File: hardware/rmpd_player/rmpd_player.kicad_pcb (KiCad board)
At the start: 2 copper layers, 99.7 x 67.9 mm, 142 parts, among them J1 POWER, J2 PROG, J3 LINE_OUT_INT_1, J4 LINE_OUT, J5 MICRO_SD, J6 POWER_INT, J7 LINE_OUT_INT_2, J8 RESERV, Q1 BC848, Q2 BC848, Q3 BC858, Q4 BC858, U1 DS3231M, U2 VS1011E, U3 LM1117-3.3, U4 ESP32-WROOM, U5 RC4558, U6 RC4558, U7 RC4558, U8 TPS54331D, U9 TPS54331D, Y1 12.288MHz

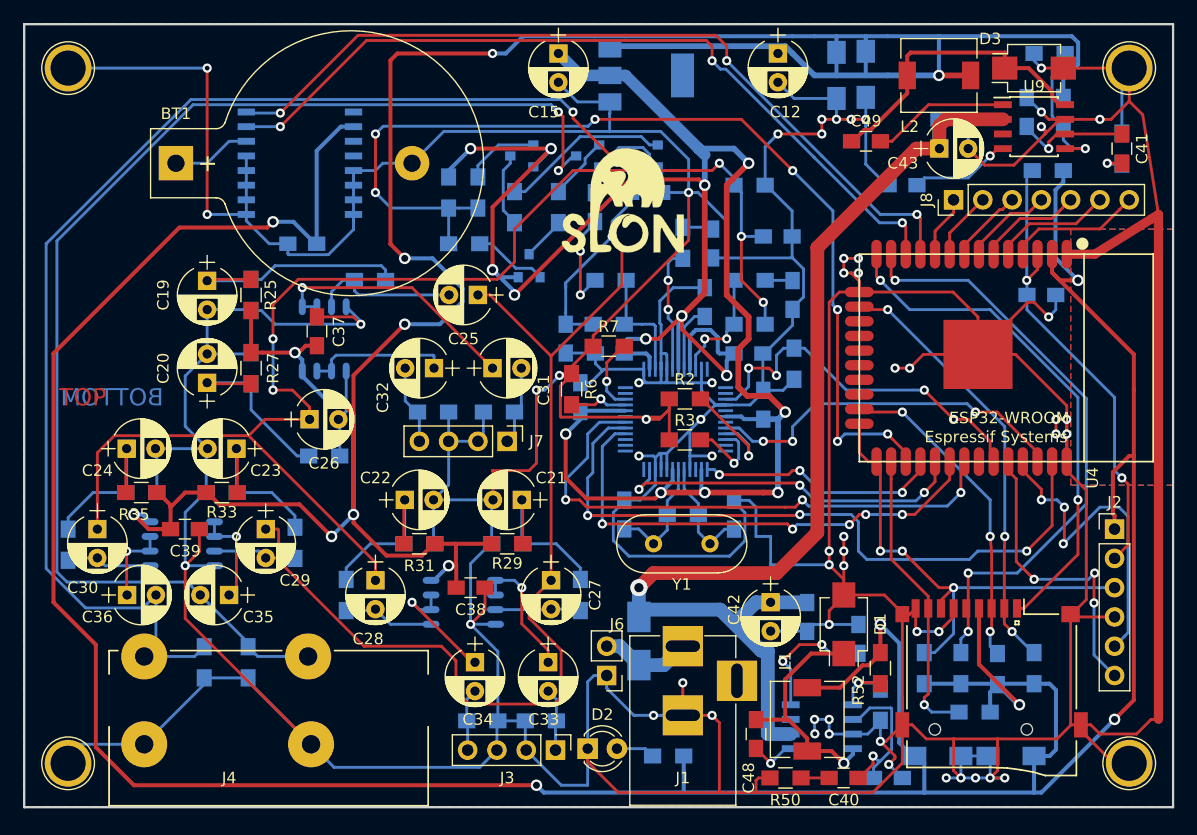
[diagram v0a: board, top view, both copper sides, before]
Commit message: update footprints to reflow
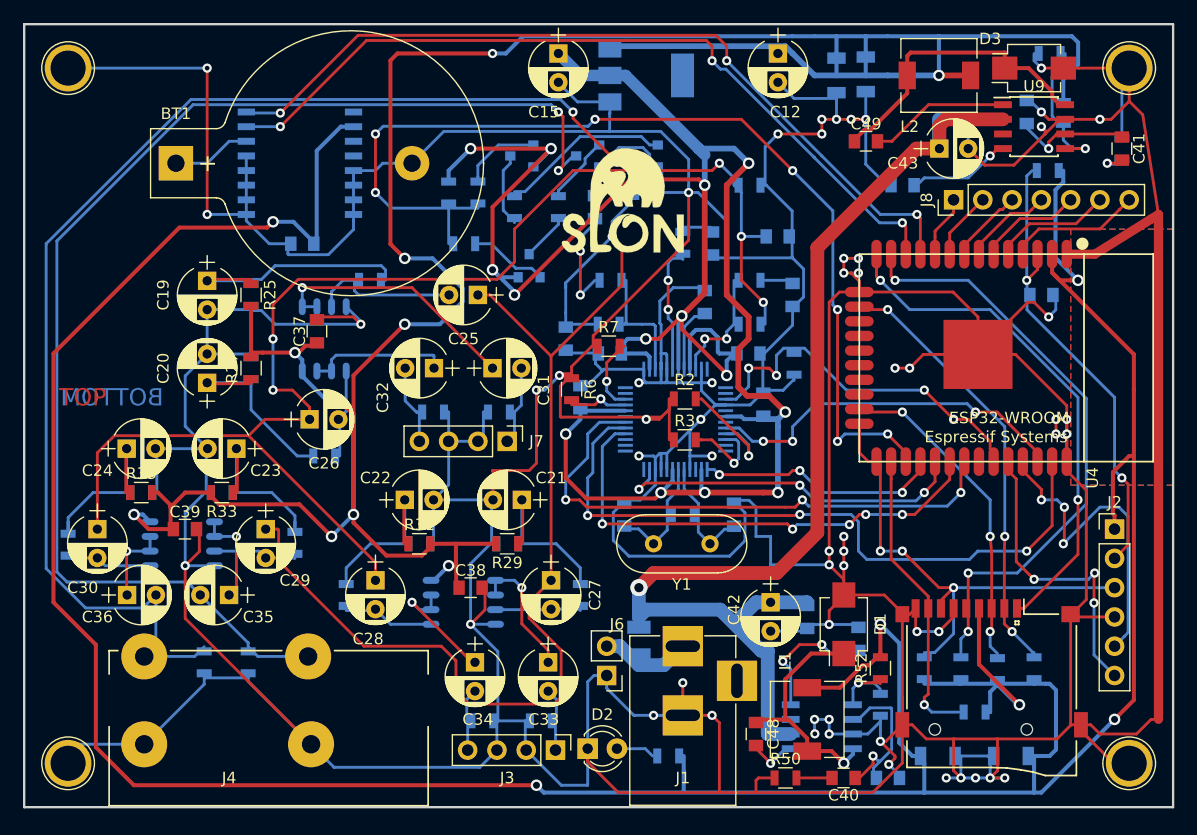
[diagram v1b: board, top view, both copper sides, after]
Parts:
- C1, C10, C11, C13, C14, C16, C2, C3, C37, C38, C39, C4, C40, C41, C44, C45, C48, C49, C5, C6, C7, C9: footprint Capacitors_SMD:C_0805_HandSoldering -> Capacitors_SMD:C_0805
- C17, C18, C46, C47: value 0.01 -> 10n; footprint Capacitors_SMD:C_0805_HandSoldering -> Capacitors_SMD:C_0805
- C50, C51, C52, C53: footprint Capacitors_SMD:C_1206_HandSoldering -> Capacitors_SMD:C_1206
- C8: value 100n -> 1uF; footprint Capacitors_SMD:C_0805_HandSoldering -> Capacitors_SMD:C_0805
- F1: footprint Fuse_Holders_and_Fuses:Fuse_SMD1206_HandSoldering -> Fuse_Holders_and_Fuses:Fuse_SMD1206_Reflow
- R1, R10, R11, R12, R13, R14, R15, R16, R17, R18, R19, R2, R20, R21, R22, R23, R24, R25, R26, R27, R28, R29, R3, R30, R31, R32, R33, R34, R35, R36, R37, R38, R39, R4, R40, R41, R42, R43, R44, R45, R46, R47, R48, R49, R5, R50, R51, R52, R53, R54, R55, R6, R7, R8, R9: footprint Resistors_SMD:R_0805_HandSoldering -> Resistors_SMD:R_0805
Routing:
- net GND: track 926.2 -> 928.2 mm
- net Net-(C24-Pad1): track 15.2 -> 16.4 mm
- net VDD_ESP: track 300.4 -> 301.6 mm
- net TRANSIENT_MUTE: track 89.0 -> 89.8 mm
- net Net-(Q4-Pad3): track 3.78 -> 4.32 mm
- net Net-(Q2-Pad1): track 5.54 -> 6.04 mm
